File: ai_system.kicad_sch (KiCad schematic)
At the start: 23 parts, among them U6 STM32N647L0H3Q

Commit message: Finalize RevB
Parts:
- C26, C27, C28, C29, C31, C32, C33, C34, C35, C36, C37, C38, C45, C46: MPN (none) -> GRM033Z71C104KE14D
- C30, C39, C40, C41, C42, C43: MPN (none) -> GRT033D70J105ME13D
- C44: MPN (none) -> GRT155D70J475ME13D
- U6: MPN (none) -> STM32N647L0H3Q; Manufacturer (none) -> STMicroelectronics
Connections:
- net GND: now also U6.V6 (VDDA18CSI)
- net VCC_MCU renamed VCC_MCU_1V8
- net VCC_MCU_1V8: no longer U6.V6 (VDDA18CSI)

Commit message: Updates for Rev. C
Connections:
- net GND: no longer U6.W2 (VREF+)
- net VCC_MCU_1V8: now also U6.W2 (VREF+)
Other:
- moved on the sheet: C27, C28, C29, C30, C31, C32, C33, C34, C35, C36, C37, C38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

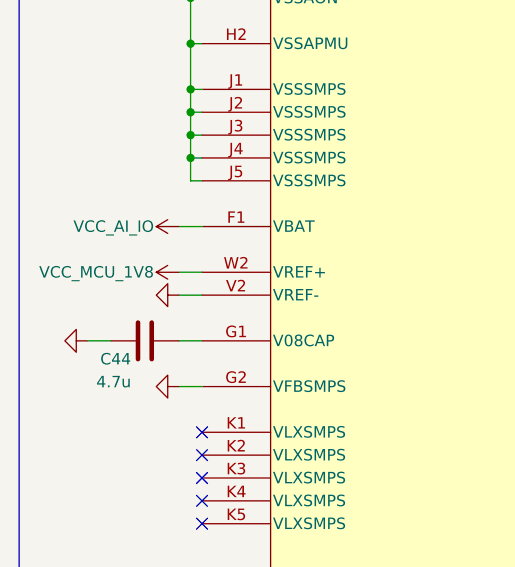
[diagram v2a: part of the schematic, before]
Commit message: Connect VREF+ to GND instead of VCC_1.8
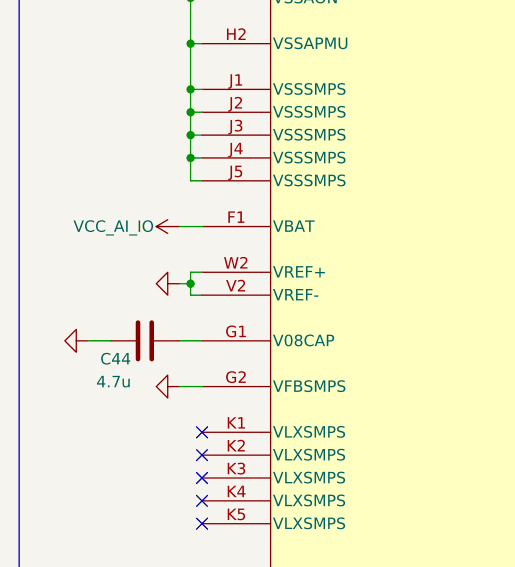
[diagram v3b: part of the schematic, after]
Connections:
- net GND: now also U6.W2 (VREF+)
- net VCC_MCU_1V8: no longer U6.W2 (VREF+)
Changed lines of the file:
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@@
 	)
 	(junction
+		(at 33.02 118.11)
+		(diameter 0)
+		(color 0 0 0 0)
+	)
+	(junction
 		(at 113.03 71.12)
 		(diameter 0)
@@
 	(wire
 		(pts
+			(xy 33.02 116.84) (xy 33.02 118.11)
+		)
+		(stroke
+			(width 0)
+			(type default)
+		)
+	)
+	(wire
+		(pts
 			(xy 90.17 104.14) (xy 91.44 104.14)
 		)
@@
 	(wire
 		(pts
+			(xy 33.02 119.38) (xy 34.29 119.38)
+		)
+		(stroke
+			(width 0)
+			(type default)
+		)
+	)
+	(wire
+		(pts
 			(xy 34.29 101.6) (xy 33.02 101.6)
 		)
@@
 	(wire
 		(pts
+			(xy 34.29 116.84) (xy 33.02 116.84)
+		)
+		(stroke
+			(width 0)
+			(type default)
+		)
+	)
+	(wire
+		(pts
 			(xy 90.17 101.6) (xy 95.25 101.6)
 		)
@@
 	(wire
 		(pts
+			(xy 33.02 118.11) (xy 33.02 119.38)
+		)
+		(stroke
+			(width 0)
+			(type default)
+		)
+	)
+	(wire
+		(pts
 			(xy 90.17 96.52) (xy 95.25 96.52)
 		)
@@
 	(wire
 		(pts
-			(xy 31.75 116.84) (xy 34.29 116.84)
-		)
-		(stroke
-			(width 0)
-			(type default)
-		)
-	)
-	(wire
-		(pts
 			(xy 95.25 101.6) (xy 95.25 106.68)
 		)
@@
 	(wire
 		(pts
-			(xy 31.75 119.38) (xy 34.29 119.38)
+			(xy 31.75 118.11) (xy 33.02 118.11)
 		)
 		(stroke
@@
 	)
 	(symbol
-		(lib_id "power:VCC")
-		(at 31.75 116.84 90)
-		(mirror x)
-		(unit 1)
-		(exclude_from_sim no)
-		(in_bom yes)
-		(on_board yes)
-		(dnp no)
-		(property "Reference" "#PWR0207"
-			(at 35.56 116.84 0)
-			(effects
-				(font
-					(size 1.27 1.27)
-				)
-				(hide yes)
-			)
-		)
-		(property "Value" "VCC_MCU_1V8"
-			(at 28.956 116.84 90)
-			(effects
-				(font
-					(size 1.27 1.27)
-				)
-				(justify left)
-			)
-		)
-		(property "Footprint" ""
-			(at 31.75 116.84 0)
-			(effects
-				(font
-					(size 1.27 1.27)
-				)
-				(hide yes)
-			)
-		)
-		(property "Datasheet" ""
-			(at 31.75 116.84 0)
-			(effects
-				(font
-					(size 1.27 1.27)
-				)
-				(hide yes)
-			)
-		)
-		(property "Description" "Power symbol creates a global label with name \"VCC\""
-			(at 31.75 116.84 0)
-			(effects
-				(font
-					(size 1.27 1.27)
-				)
-				(hide yes)
-			)
-		)
-		(pin "1"
-		)
-		(instances
-			(project "hw"
-				(path "/37690768-e2be-4a37-b8f7-45d5da107609/848c734b-5721-4fc9-aed5-8e152bafb038"
-					(reference "#PWR0207")
-					(unit 1)
-				)
-			)
-		)
-	)
-	(symbol
 		(lib_id "power:GND")
 		(at 96.52 115.57 90)
@@
 	(symbol
 		(lib_id "power:GND")
-		(at 31.75 119.38 270)
+		(at 31.75 118.11 270)
 		(unit 1)
 		(exclude_from_sim no)
@@
 		(fields_autoplaced yes)
 		(property "Reference" "#PWR051"
-			(at 25.4 119.38 0)
+			(at 25.4 118.11 0)
 			(effects
 				(font
@@
 		)
 		(property "Value" "GND"
-			(at 27.94 119.3799 90)
+			(at 27.94 118.1099 90)
 			(effects
 				(font
@@
 		)
 		(property "Footprint" ""
-			(at 31.75 119.38 0)
+			(at 31.75 118.11 0)
 			(effects
 				(font
@@
 		)
 		(property "Datasheet" ""
-			(at 31.75 119.38 0)
+			(at 31.75 118.11 0)
 			(effects
 				(font
@@
 		)
 		(property "Description" "Power symbol creates a global label with name \"GND\" , ground"
-			(at 31.75 119.38 0)
+			(at 31.75 118.11 0)
 			(effects
 				(font
